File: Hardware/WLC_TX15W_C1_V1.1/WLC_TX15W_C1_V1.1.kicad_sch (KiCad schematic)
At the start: 129 parts, among them J1 Conn_01x05, J2 PWR, Q1 BSZ0910LS, Q2 BSZ0910LS, Q3 BSZ0910LS, Q4 BSS138, Q5 BSZ0910LS, Q6 BSZ0910LS, Q7 BSZ0910LS, Q8 BSS138, Q9 AO3400A, U2 LM358, U3 SLS32AIA020X2USON10XTMA4, U4 WLC1115-68LQXQ, Y2 SG-210STF

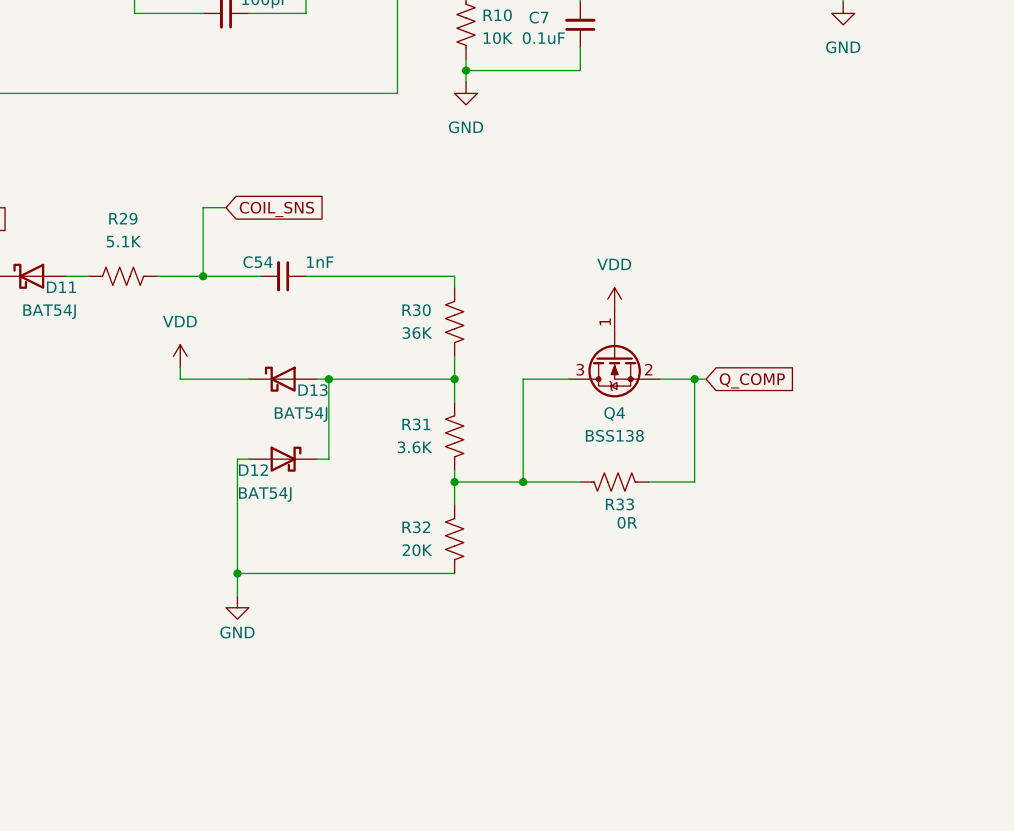
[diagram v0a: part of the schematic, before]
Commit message: add simplified diagram
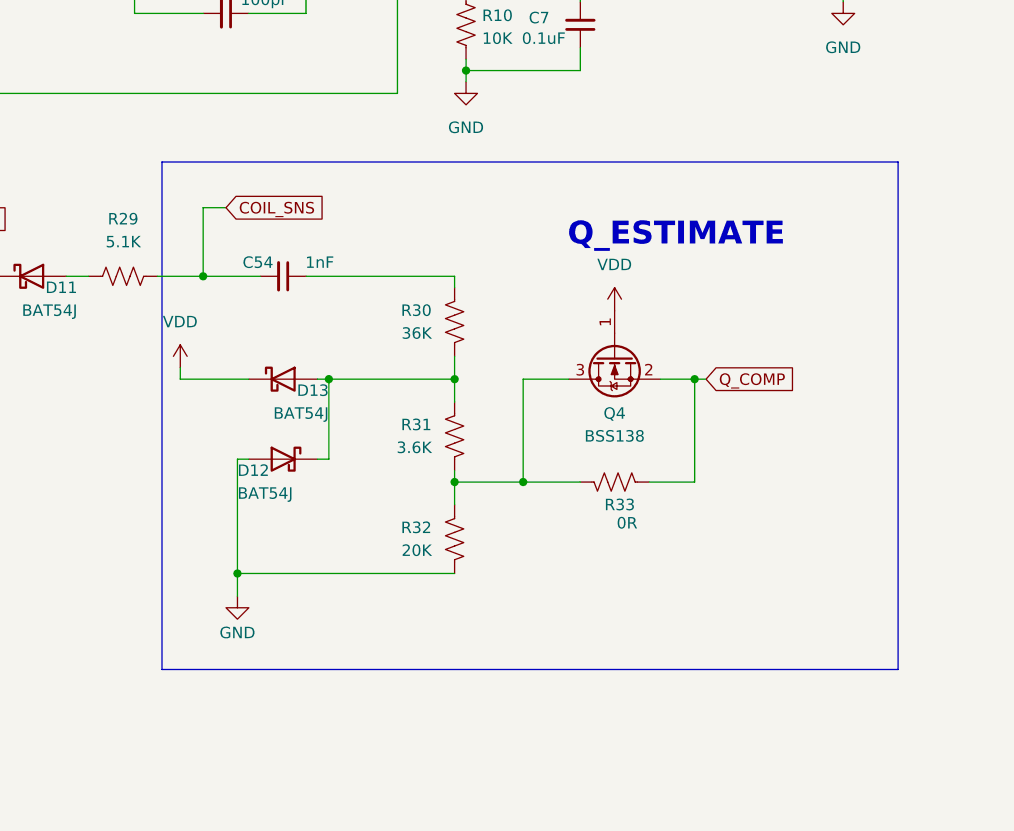
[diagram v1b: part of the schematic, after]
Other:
- note added: "Q_ESTIMATE"
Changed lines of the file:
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@@
+		)
+	)
+	(rectangle
+		(start 310.388 158.75)
+		(end 392.176 215.138)
+		(stroke
+			(width 0)
+			(type default)
+		)
+		(fill
+			(type none)
 		)
 	)
@@
 		(effects
 			(font
+				(size 2.54 2.54)
+				(thickness 0.508)
+				(bold yes)
+			)
+		)
+	)
+	(text "Q_ESTIMATE"
+		(exclude_from_sim no)
+		(at 367.538 166.878 0)
+		(effects
+			(font

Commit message: add usb type c
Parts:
- removed D12, D13: BAT54J, Diode_SMD:D_SOD-323F, symbol Diode:BAT54J
- removed J2: PWR, TerminalBlock:TerminalBlock_bornier-2_P5.08mm, symbol Connector_Generic:Conn_01x02
- removed Q4: BSS138, Package_TO_SOT_SMD:SOT-23, symbol Transistor_FET:BSS138
- removed R33: 0R, Resistor_SMD:R_0603_1608Metric, symbol Device:R_US
- added C61: 0.1uF, Capacitor_SMD:C_0402_1005Metric, symbol Device:C_Small
- added D15: MMBD1503, Package_TO_SOT_SMD:SOT-23, symbol haidv_library:MMBD1503
- added J3: USB4105-GF-A, Footprints-Models:GCT_USB4105-GF-A, symbol USB4105-GF-A:USB4105-GF-A
- added TP3: VIN+, TestPoint:TestPoint_Loop_D3.50mm_Drill1.4mm_Beaded, symbol Connector:TestPoint
- added TP4: VIN-, TestPoint:TestPoint_Loop_D3.50mm_Drill1.4mm_Beaded, symbol Connector:TestPoint
- added TP5, TP6, TP7, TP8: GND, TestPoint:TestPoint_Plated_Hole_D3.0mm, symbol Connector:TestPoint
- C16, C17, C18, C19, C20: footprint Capacitor_SMD:C_0805_2012Metric -> Capacitor_SMD:C_1206_3216Metric
- C2, C23, C24, C25, C26, C31, C32: footprint Capacitor_SMD:C_0603_1608Metric -> Capacitor_SMD:C_0402_1005Metric
- C6: value 100pF -> 150pF
- D10, D4, D5, D6, D7, D9: value BAT54J -> 1PS76SB21
- D11: value BAT54J -> BAS16H; footprint Diode_SMD:D_SOD-323F -> Diode_SMD:D_SOD-123F
- R18, R3, R4, R6, TH1: footprint Resistor_SMD:R_0603_1608Metric -> Resistor_SMD:R_0402_1005Metric
- R22: value 0R -> 5.1K; footprint Resistor_SMD:R_0603_1608Metric -> Resistor_SMD:R_0402_1005Metric
- R9: value 1M -> 5.1K; footprint Resistor_SMD:R_0603_1608Metric -> Resistor_SMD:R_0402_1005Metric
- TH2: footprint Connector_PinHeader_2.54mm:PinHeader_1x02_P2.54mm_Vertical -> Resistor_SMD:R_0805_2012Metric
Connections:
- net ASK_DEMOD: no longer R9.1
- net ASK_TST: now also U4.42 (ASK_TST); no longer R22.1
- net CC1_0: now also R22.2, J3.A5 (CC1)
- net CC2_0: now also R9.2, J3.B5 (CC2)
- net D+_0: now also J3.A6 (DP1), J3.B6 (DP2)
- net D-_0: now also J3.A7 (DN1), J3.B7 (DN2)
- net GND: now also R22.1, R9.1, C61.1, D15.1 (A), TP5.1, TP6.1, TP7.1, TP8.1
- net IOUT_CSN_0: now also C61.2
- net Q_COMP: now also R31.2, R32.1
- net VDD: now also D15.2 (K)
- net at C3.2, D5.1 (K), R11.2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: now also D4.2 (A); no longer D4.1 (K)
- net USB-GND: now reaches C9.1, D8.1 (A1), FL1.4, R35.2
- net USB-GND: now also J3.A1_B12 (GND), J3.B1_A12 (GND__1), J3.SH1 (SHELL_GND), J3.SH2 (SHELL_GND__1), J3.SH3 (SHELL_GND__2), J3.SH4 (SHELL_GND__3), TP4.1
- net at C6.1, R8.1, U2.1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: no longer R9.2
- net at C5.1, D5.2 (A), R7.2: now also D4.1 (K); no longer D4.2 (A)
- net USB-IN: now reaches D8.2 (A2), Q9.2 (S)
- net USB-IN: now also J3.A4_B9 (VBUS), J3.B4_A9 (VBUS__1), TP3.1
- net at R30.2, R31.1: now also D15.3 (common)
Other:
- note added: "CLOCK GENERATION"
- note added: "TYPE C"
- moved on the sheet: C10, C11, C12, C13, C21, C22, C28, C3, C38, C39, C55, C56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

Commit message: update bom
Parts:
- removed TP1: P3.3, TestPoint:TestPoint_Pad_D1.0mm, symbol Connector:TestPoint
- removed TP2: ASK_TST, TestPoint:TestPoint_Pad_D1.0mm, symbol Connector:TestPoint
- C2, C23, C24, C35, C50, C51: footprint Capacitor_SMD:C_0402_1005Metric -> Capacitor_SMD:C_0603_1608Metric
- C3, C33, C4, C5: footprint Capacitor_SMD:C_0603_1608Metric -> Capacitor_SMD:C_0402_1005Metric
- L1: footprint Inductor_SMD:L_Bourns_SRP1050WA -> Inductor_SMD:L_Bourns-SRN8040_8x8.15mm
- R14, R15, R16, R17: footprint Capacitor_SMD:C_0402_1005Metric -> Resistor_SMD:R_0402_1005Metric
- R19, R20, R23, R24, R27, R28, R29, R5, R7: footprint Resistor_SMD:R_0603_1608Metric -> Resistor_SMD:R_0402_1005Metric
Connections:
- net ASK_TST: no longer names the net of U4.42 (ASK_TST)
- net P3.3: no longer names the net of U4.59 (GPIO12)

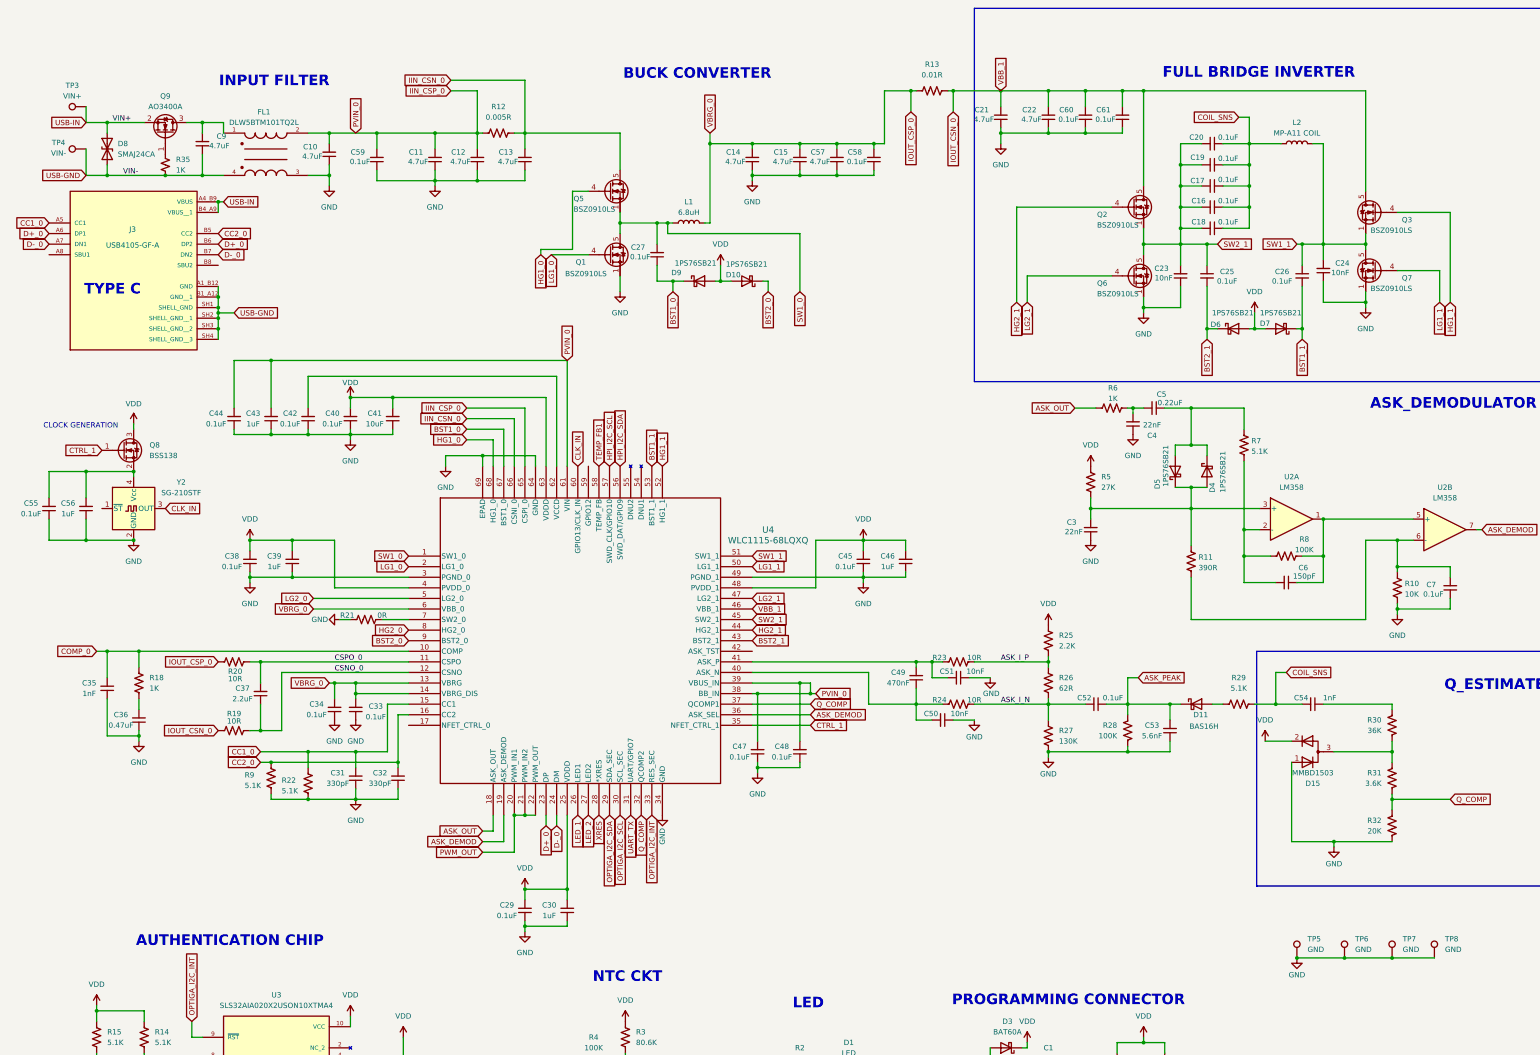
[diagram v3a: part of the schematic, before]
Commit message: Fix board outline
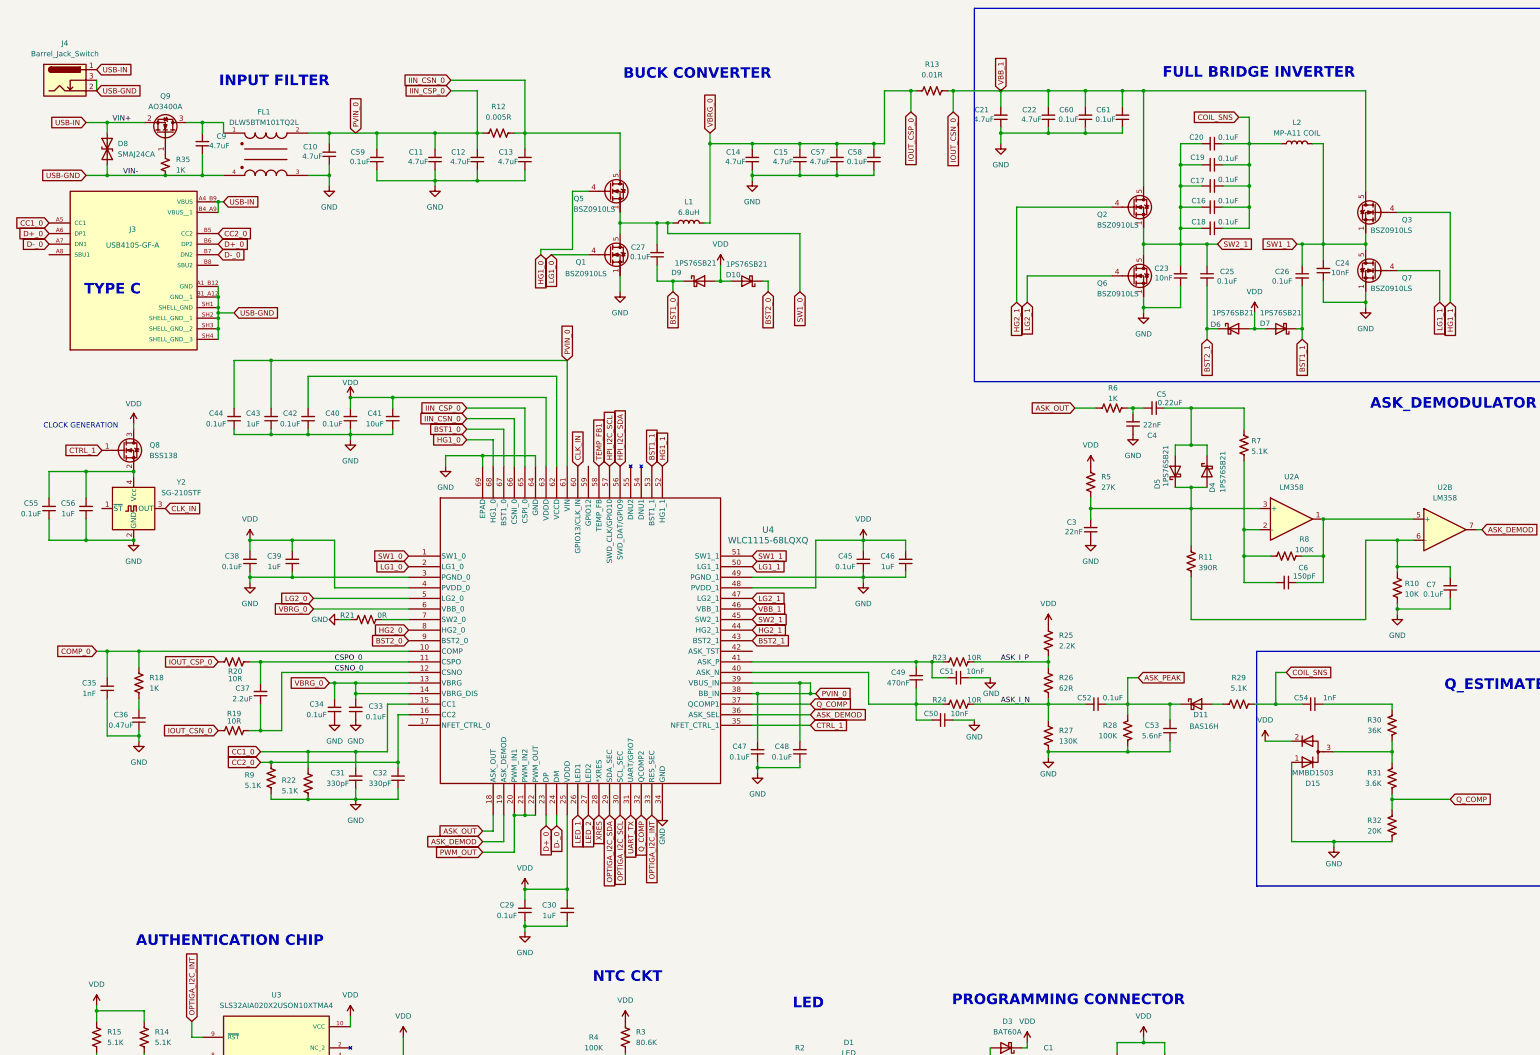
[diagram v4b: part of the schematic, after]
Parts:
- removed TP3: VIN+, TestPoint:TestPoint_Loop_D3.50mm_Drill1.4mm_Beaded, symbol Connector:TestPoint
- removed TP4: VIN-, TestPoint:TestPoint_Loop_D3.50mm_Drill1.4mm_Beaded, symbol Connector:TestPoint
- removed TP5, TP6, TP7, TP8: GND, TestPoint:TestPoint_Plated_Hole_D3.0mm, symbol Connector:TestPoint
- added J4: Barrel_Jack_Switch, Connector_BarrelJack:BarrelJack_GCT_DCJ200-10-A_Horizontal, symbol Connector:Barrel_Jack_Switch
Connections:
- net USB-GND: now also J4.2, J4.3
- net USB-IN: now also J4.1
